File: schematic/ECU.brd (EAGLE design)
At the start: 25 x 79 mm, 29 parts, among them J1 Break, J2 COMM, J3 PWR, J4 DISPLAY, J5 THROTTLE, J6 LED, J7 SPEED, Q1 NMOSFETSOT23, Q5 NMOSFETSOT23, U1 Arduino Nano Every

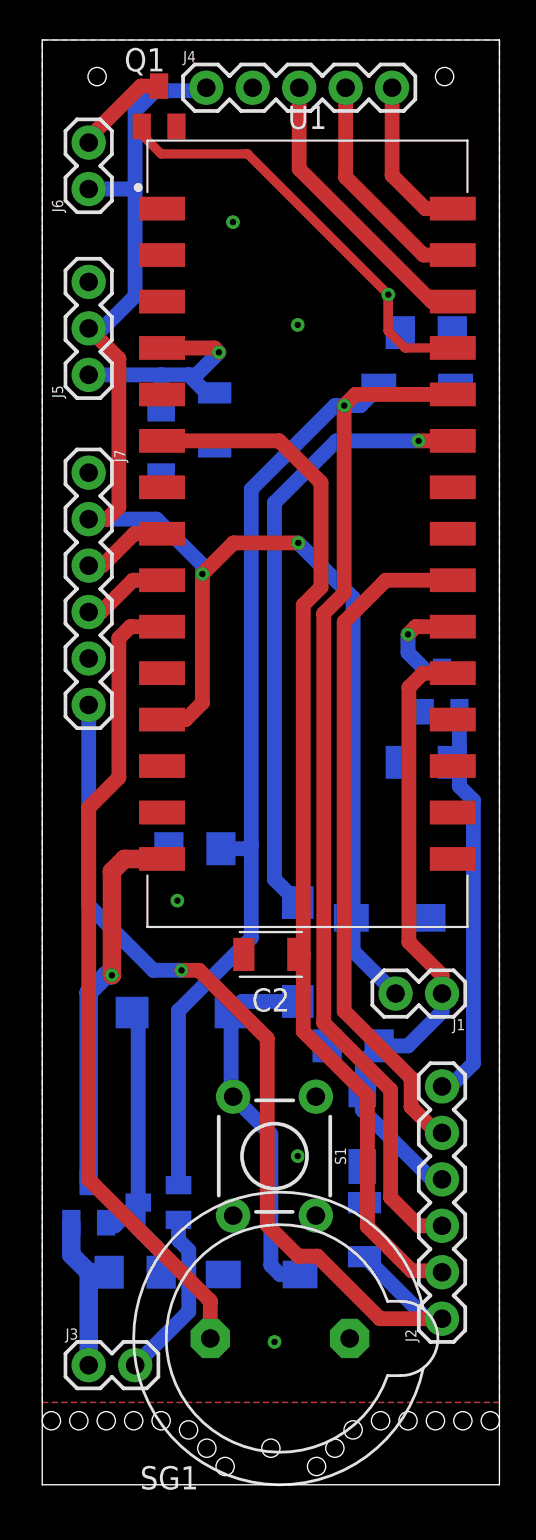
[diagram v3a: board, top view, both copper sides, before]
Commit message: Fix minor issues in PCB
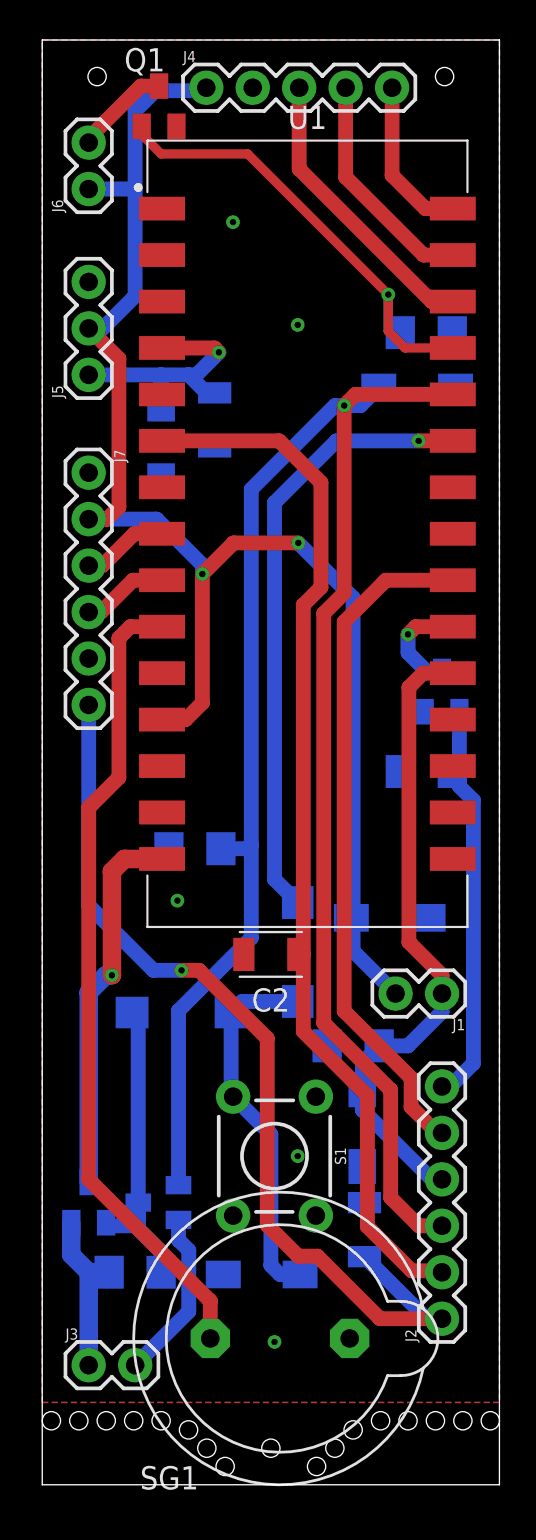
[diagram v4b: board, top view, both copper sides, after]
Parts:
- moved R4 0.50 mm to (21.0, 39.0)
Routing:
- net N$2: track 17.2 -> 18.0 mm
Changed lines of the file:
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@@
 <layers>
 <layer number="1" name="Top" color="4" fill="1" visible="yes" active="yes"/>
-<layer number="16" name="Bottom" color="1" fill="1" visible="yes" active="yes"/>
+<layer number="16" name="Bottom" color="1" fill="1" visible="no" active="yes"/>
 <layer number="17" name="Pads" color="2" fill="1" visible="yes" active="yes"/>
 <layer number="18" name="Vias" color="2" fill="1" visible="yes" active="yes"/>
@@
 <layer number="20" name="Dimension" color="24" fill="1" visible="yes" active="yes"/>
 <layer number="21" name="tPlace" color="7" fill="1" visible="yes" active="yes"/>
-<layer number="22" name="bPlace" color="7" fill="1" visible="yes" active="yes"/>
+<layer number="22" name="bPlace" color="7" fill="1" visible="no" active="yes"/>
 <layer number="23" name="tOrigins" color="15" fill="1" visible="yes" active="yes"/>
-<layer number="24" name="bOrigins" color="15" fill="1" visible="yes" active="yes"/>
+<layer number="24" name="bOrigins" color="15" fill="1" visible="no" active="yes"/>
 <layer number="25" name="tNames" color="7" fill="1" visible="yes" active="yes"/>
-<layer number="26" name="bNames" color="7" fill="1" visible="yes" active="yes"/>
+<layer number="26" name="bNames" color="7" fill="1" visible="no" active="yes"/>
 <layer number="27" name="tValues" color="7" fill="1" visible="no" active="yes"/>
 <layer number="28" name="bValues" color="7" fill="1" visible="no" active="yes"/>
@@
 <layer number="38" name="bTest" color="7" fill="1" visible="no" active="yes"/>
 <layer number="39" name="tKeepout" color="4" fill="11" visible="yes" active="yes"/>
-<layer number="40" name="bKeepout" color="1" fill="11" visible="yes" active="yes"/>
+<layer number="40" name="bKeepout" color="1" fill="11" visible="no" active="yes"/>
 <layer number="41" name="tRestrict" color="4" fill="10" visible="yes" active="yes"/>
-<layer number="42" name="bRestrict" color="1" fill="10" visible="yes" active="yes"/>
+<layer number="42" name="bRestrict" color="1" fill="10" visible="no" active="yes"/>
 <layer number="43" name="vRestrict" color="2" fill="10" visible="no" active="yes"/>
 <layer number="44" name="Drills" color="7" fill="1" visible="no" active="yes"/>
@@
 <layer number="50" name="dxf" color="7" fill="1" visible="no" active="no"/>
 <layer number="51" name="tDocu" color="7" fill="1" visible="yes" active="yes"/>
-<layer number="52" name="bDocu" color="7" fill="1" visible="yes" active="yes"/>
+<layer number="52" name="bDocu" color="7" fill="1" visible="no" active="yes"/>
 <layer number="53" name="tGND_GNDA" color="7" fill="9" visible="no" active="no"/>
 <layer number="54" name="bGND_GNDA" color="1" fill="9" visible="no" active="no"/>
@@
 <attribute name="MANUFACTURER" value="" x="-44.45" y="69.77" size="1.778" layer="28" rot="MR90" display="off"/>
 <attribute name="MPN" value="" x="-44.45" y="69.77" size="1.778" layer="28" rot="MR90" display="off"/>
-<attribute name="NAME" x="16.08" y="29.13" size="1.27" layer="26" rot="MR90" align="bottom-center"/>
+<attribute name="NAME" x="10.58" y="29.63" size="1.27" layer="26" rot="MR90" align="bottom-center"/>
 <attribute name="OPERATING_TEMP" value="" x="-44.45" y="69.77" size="1.778" layer="28" rot="MR90" display="off"/>
 <attribute name="PART_STATUS" value="" x="-44.45" y="69.77" size="1.778" layer="28" rot="MR90" display="off"/>
@@
 <attribute name="MANUFACTURER" value="" x="64.77" y="-4.89" size="1.778" layer="28" rot="MR270" display="off"/>
 <attribute name="MPN" value="" x="64.77" y="-4.89" size="1.778" layer="28" rot="MR270" display="off"/>
-<attribute name="NAME" x="4.445" y="17.335" size="1.27" layer="26" rot="MR270"/>
+<attribute name="NAME" x="5.445" y="18.835" size="1.27" layer="26" rot="MR180"/>
 <attribute name="OPERATING_TEMP" value="" x="64.77" y="-4.89" size="1.778" layer="28" rot="MR270" display="off"/>
 <attribute name="PART_STATUS" value="" x="64.77" y="-4.89" size="1.778" layer="28" rot="MR270" display="off"/>
@@
 <attribute name="MANUFACTURER" value="ON Semiconductor" x="-22.86" y="-42.99" size="1.778" layer="28" rot="MR0" display="off"/>
 <attribute name="MPN" value="BSS84" x="-22.86" y="-42.99" size="1.778" layer="28" rot="MR0" display="off"/>
-<attribute name="NAME" x="4.445" y="17.335" size="1.27" layer="26" rot="MR0"/>
+<attribute name="NAME" x="3.445" y="17.335" size="1.27" layer="26" rot="MR0"/>
 <attribute name="OPERATING_TEMP" value="" x="-22.86" y="-42.99" size="1.778" layer="28" rot="MR0" display="off"/>
 <attribute name="PART_STATUS" value="" x="-22.86" y="-42.99" size="1.778" layer="28" rot="MR0" display="off"/>
@@
 </element>
 <element name="R1" library="eagle-ltspice" library_urn="urn:adsk.eagle:library:217" package="R1206" package3d_urn="urn:adsk.eagle:package:13301/1" value="10K" x="8.35" y="34.78" smashed="yes" rot="MR180">
-<attribute name="NAME" x="7.08" y="33.51" size="1.27" layer="26" rot="MR180"/>
+<attribute name="NAME" x="7.08" y="37.01" size="1.27" layer="26" rot="MR180"/>
 <attribute name="SPICEMODEL" value="NONE" x="56.61" y="86.85" size="1.778" layer="28" rot="MR180" display="off"/>
 <attribute name="SPICEPREFIX" value="R" x="56.61" y="86.85" size="1.778" layer="28" rot="MR180" display="off"/>
@@
 </element>
 <element name="D6" library="eScooter" package="DIOM5027X220N" package3d_urn="urn:adsk.eagle:package:21928182/1" value="TVS_DIODESMA" x="19" y="31" smashed="yes" rot="MR180">
-<attribute name="NAME" x="19" y="29.015" size="1.27" layer="26" rot="MR180" align="bottom-center"/>
+<attribute name="NAME" x="19" y="34.015" size="1.27" layer="26" rot="MR180" align="bottom-center"/>
 <attribute name="VALUE" x="19" y="32.985" size="1.27" layer="28" rot="MR180" align="top-center"/>
 </element>
@@
 <attribute name="VALUE" x="12" y="13.485" size="1.27" layer="28" rot="MR180" align="top-center"/>
 </element>
-<element name="R4" library="eagle-ltspice" library_urn="urn:adsk.eagle:library:217" package="R1206" package3d_urn="urn:adsk.eagle:package:13301/1" value="10K" x="21" y="39.5" smashed="yes" rot="MR180">
-<attribute name="NAME" x="19.73" y="38.23" size="1.27" layer="26" rot="MR180"/>
-<attribute name="SPICEMODEL" value="NONE" x="21" y="39.5" size="1.778" layer="28" rot="MR180" display="off"/>
-<attribute name="SPICEPREFIX" value="R" x="21" y="39.5" size="1.778" layer="28" rot="MR180" display="off"/>
-<attribute name="VALUE" x="19.73" y="42.04" size="1.27" layer="28" rot="MR180"/>
+<element name="R4" library="eagle-ltspice" library_urn="urn:adsk.eagle:library:217" package="R1206" package3d_urn="urn:adsk.eagle:package:13301/1" value="10K" x="21" y="39" smashed="yes" rot="MR180">
+<attribute name="NAME" x="19.73" y="37.73" size="1.27" layer="26" rot="MR180"/>
+<attribute name="SPICEMODEL" value="NONE" x="21" y="39" size="1.778" layer="28" rot="MR180" display="off"/>
+<attribute name="SPICEPREFIX" value="R" x="21" y="39" size="1.778" layer="28" rot="MR180" display="off"/>
+<attribute name="VALUE" x="19.73" y="41.54" size="1.27" layer="28" rot="MR180"/>
 </element>
 <element name="R5" library="eagle-ltspice" library_urn="urn:adsk.eagle:library:217" package="R1206" package3d_urn="urn:adsk.eagle:package:13301/1" value="10K" x="21" y="63" smashed="yes" rot="MR0">
@@
 <wire x1="22.3076" y1="21.78" x2="21.86" y2="21.78" width="0.8128" layer="16"/>
 <wire x1="22.81" y1="38.19" x2="23.5776" y2="37.4224" width="0.8128" layer="16"/>
-<wire x1="22.81" y1="42.27" x2="22.81" y2="39.5" width="0.8128" layer="16"/>
-<wire x1="22.81" y1="39.5" x2="22.81" y2="38.19" width="0.8128" layer="16"/>
+<wire x1="22.81" y1="42.27" x2="22.81" y2="39" width="0.8128" layer="16"/>
+<wire x1="22.81" y1="39" x2="22.81" y2="38.19" width="0.8128" layer="16"/>
 <wire x1="23.5776" y1="37.4224" x2="23.5776" y2="23.05" width="0.8128" layer="16"/>
 <contactref element="R4" pad="2"/>
-<wire x1="22.422" y1="39.5" x2="22.81" y2="39.5" width="0.8128" layer="16"/>
+<wire x1="22.422" y1="39" x2="22.81" y2="39" width="0.8128" layer="16"/>
 </signal>
 <signal name="LEDCTL">
@@
 <contactref element="D2" pad="2"/>
 <wire x1="3.49" y1="14.33" x2="3.66" y2="14.16" width="0.8128" layer="16"/>
-<wire x1="3.98" y1="14.16" x2="5.25" y2="15.43" width="0.8128" layer="16"/>
-<wire x1="3.66" y1="14.16" x2="3.98" y2="14.16" width="0.8128" layer="16"/>
+<wire x1="5.25" y1="14.16" x2="5.25" y2="15.43" width="0.8128" layer="16"/>
+<wire x1="3.66" y1="14.16" x2="5.25" y2="14.16" width="0.8128" layer="16"/>
 <wire x1="5.25" y1="15.43" x2="5.25" y2="13.99" width="0.8128" layer="16"/>
 <wire x1="6.502" y1="12.738" x2="6.502" y2="11.62" width="0.8128" layer="16"/>

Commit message: Change MAX regulator package
- Change MAX package to drill-pin
- Move button to bottom layout
- Move elements for better work on regulator and ECU
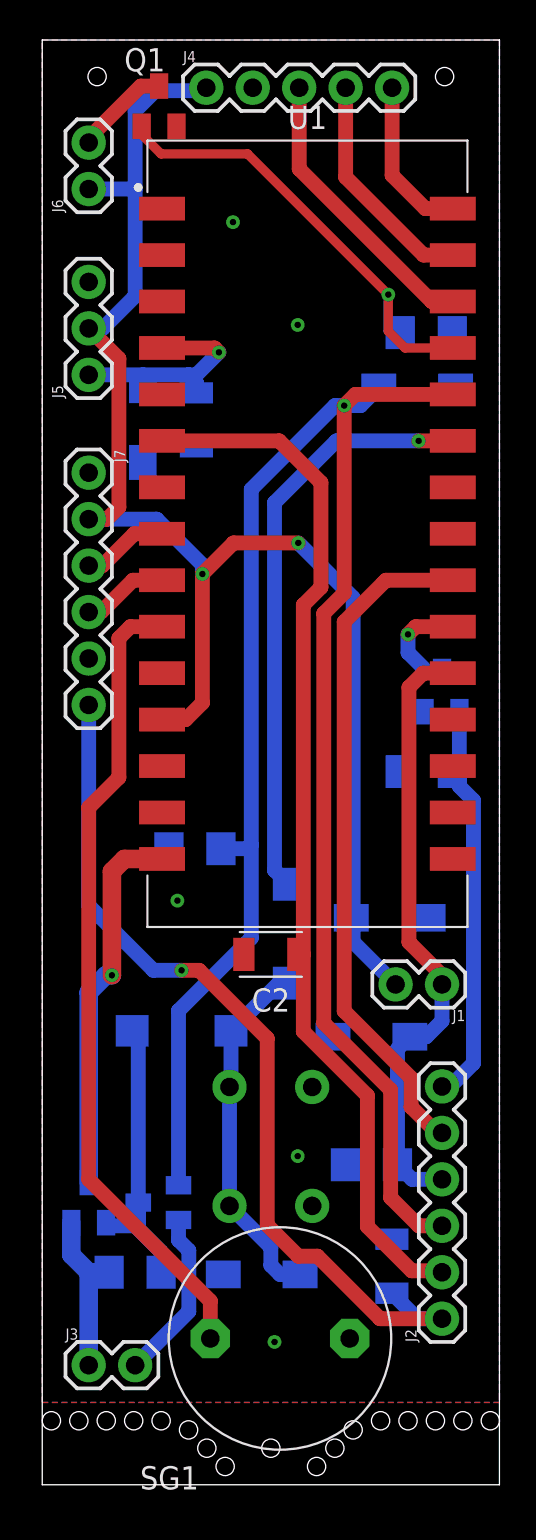
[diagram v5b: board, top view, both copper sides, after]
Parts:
- S1: value (none) -> MOMENTARY-SWITCH-SPST-PTH-6.0MM
- moved R3 6.58 mm to (18.0, 17.5)
- moved D5 5.02 mm to (18.0, 24.5), turned to 180 degrees
- moved C3 2.50 mm to (19.1, 11.9)
- moved D4 1.41 mm to (5.50, 58.0)
- moved D3 1.12 mm to (13.5, 30.1)
- moved C1 1.00 mm to (8.43, 58.2)
- moved D2 1.00 mm to (7.62, 24.8)
- moved S1 0.57 mm to (12.5, 18.5), flipped to the bottom, turned to 90 degrees
- moved J1 0.50 mm to (21.9, 27.4)
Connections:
- net GND: now also S1.2
- net N$5: now also S1.4
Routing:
- net SPOUT: track 51.3 -> 48.9 mm
- net THIN: track 14.3 -> 12.6 mm
- net BTN: track 33.5 -> 32.3 mm
- net N$2: track 18.0 -> 17.0 mm
- net ST: track 35.2 -> 34.4 mm
- net 5V: track 83.0 -> 82.5 mm

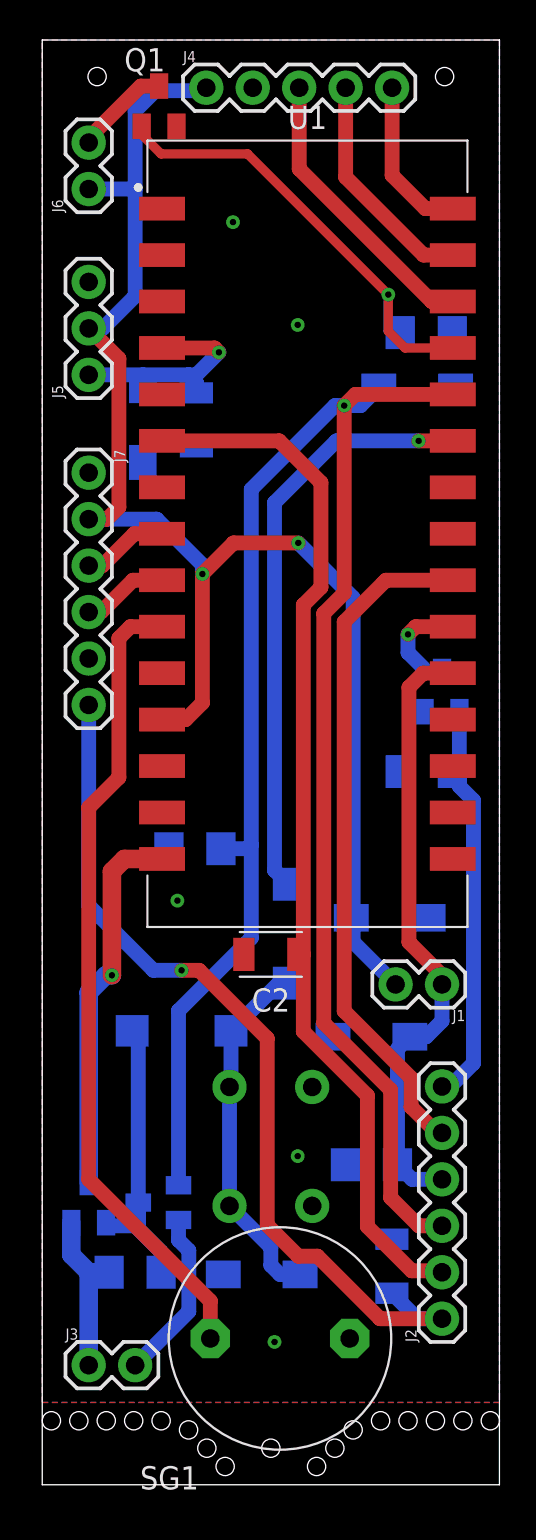
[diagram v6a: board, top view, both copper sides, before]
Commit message: Rework ECU board
- Align sizes
- Align elements placement on layers
- Change power traces in regulator
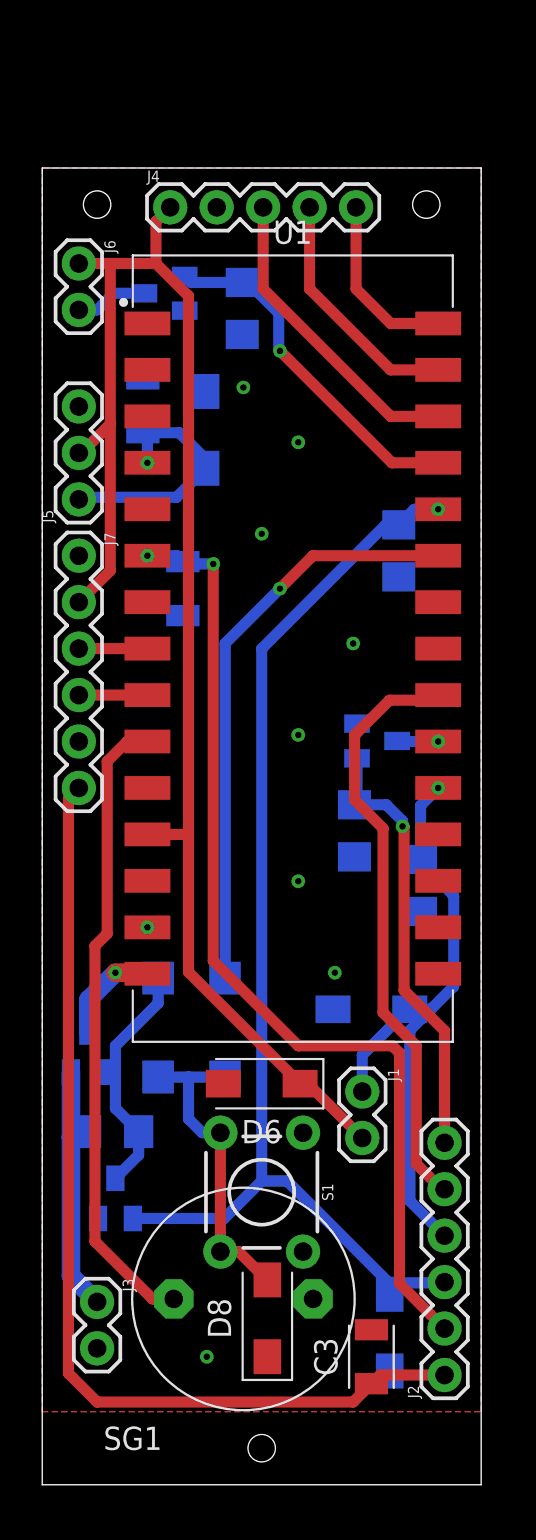
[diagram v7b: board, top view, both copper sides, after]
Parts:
- moved D7 51.7 mm to (19.0, 8.32), turned to 270 degrees
- moved C2 20.6 mm to (7.69, 49.0), flipped to the bottom, turned to 270 degrees
- moved R1 19.7 mm to (19.5, 51.1), turned to 90 degrees
- moved R3 15.5 mm to (20.7, 32.8), turned to 270 degrees
- moved D6 11.5 mm to (12.0, 21.9), flipped to the top
- moved Q1 10.2 mm to (6.69, 65.2), flipped to the bottom, turned to 270 degrees
- moved R5 10.2 mm to (10.9, 64.3), turned to 90 degrees
- moved Q4 8.23 mm to (2.52, 23.7)
- moved R2 7.79 mm to (3.85, 19.3)
- moved J1 7.30 mm to (17.5, 21.5), turned to 270 degrees
- moved J5 6.83 mm to (2.00, 53.9)
- moved J4 6.83 mm to (7.00, 69.8)
- moved U1 6.33 mm to (13.7, 45.7)
- moved D3 6.19 mm to (10.0, 25.0)
- moved R4 5.09 mm to (17.1, 35.8), turned to 90 degrees
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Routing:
- net PWM: track 105.7 -> 62.9 mm
- net VIN: track 20.8 -> 5.63 mm
- net SPK: track 44.3 -> 34.8 mm
- net GND: track 9.39 -> 0.00 mm, vias 5 -> 9
- net LEDCTL: track 26.2 -> 19.3 mm
- net SPOUT: track 48.9 -> 54.1 mm, vias 1 -> 0
- net STLEDCTL: track 37.2 -> 32.4 mm
- net 12V: track 9.61 -> 14.1 mm
- net BAT: track 57.6 -> 53.9 mm, vias 0 -> 2
- net SP: track 5.91 -> 2.25 mm
- net N$2: track 17.0 -> 13.7 mm
- net N$5: track 20.2 -> 17.7 mm
- net SPIN: track 22.2 -> 24.3 mm, vias 0 -> 1
- net 5V: track 82.5 -> 84.2 mm, vias 2 -> 0
- net N$1: track 5.37 -> 3.97 mm
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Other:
- board size 25 x 79 mm -> 24 x 72 mm

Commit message: Remove high-side switch for driver
- Keep driver alway on for now
- Add mosfet switched for speed and throttle
- Align break work
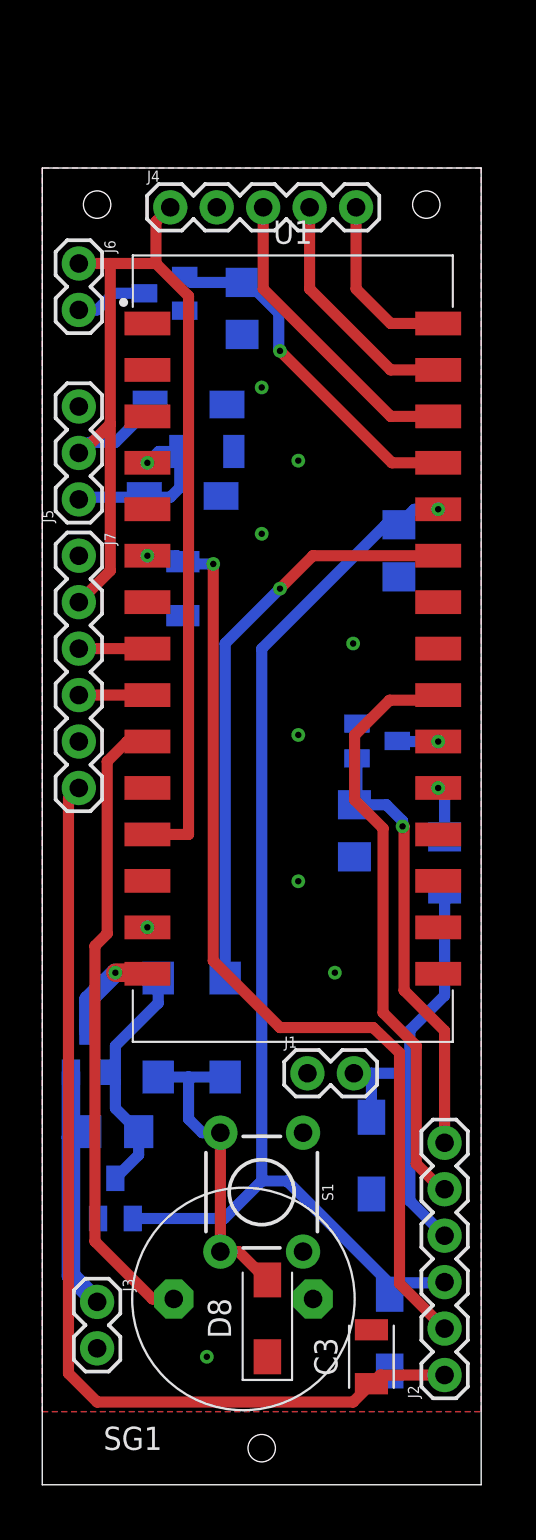
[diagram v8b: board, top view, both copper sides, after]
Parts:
- removed D5: TVS_DIODESMA, eScooter:DIOM5027X220N
- added D1: TVS_DIODESMA, eScooter:DIOM5027X220N
- moved D6 37.4 mm to (8.00, 59.1), flipped to the bottom
- moved C1 4.30 mm to (9.00, 56.5), turned to 0 degrees
- moved D4 3.82 mm to (7.68, 54.1), turned to 0 degrees
- moved J1 3.16 mm to (14.5, 22.5), turned to 0 degrees
- moved R3 1.80 mm to (22.0, 34.0)
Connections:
- net PWM renamed PWON
- net SPIN renamed SPEED
- net SPOUT renamed THCTL
- new net STCTL: D1.2, J1.2, J2.4, R3.2
- net 5V: no longer J1.2
- net GND: now also D1.1, J1.1; no longer D5.1, R3.2
- net ST: no longer D5.2, J1.1, J2.4
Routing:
- net ST: track 34.1 -> 2.82 mm
- net STCTL: track 0.00 -> 26.0 mm
- net 5V: track 84.2 -> 68.5 mm
- net THIN: track 13.9 -> 10.7 mm
